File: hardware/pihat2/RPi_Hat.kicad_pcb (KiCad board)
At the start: 2 copper layers, 65 x 56.5 mm, 48 parts, among them J2 RPi_GPIO, P1 USB_OTG, P2 BATT, P3 THERM, U1 MCP73833, U2 SMA_Edge_Mount, U3 SMA_Edge_Mount, U4 TPS61027, U5 MCP3021, U6 Si4464, X1 30MHz

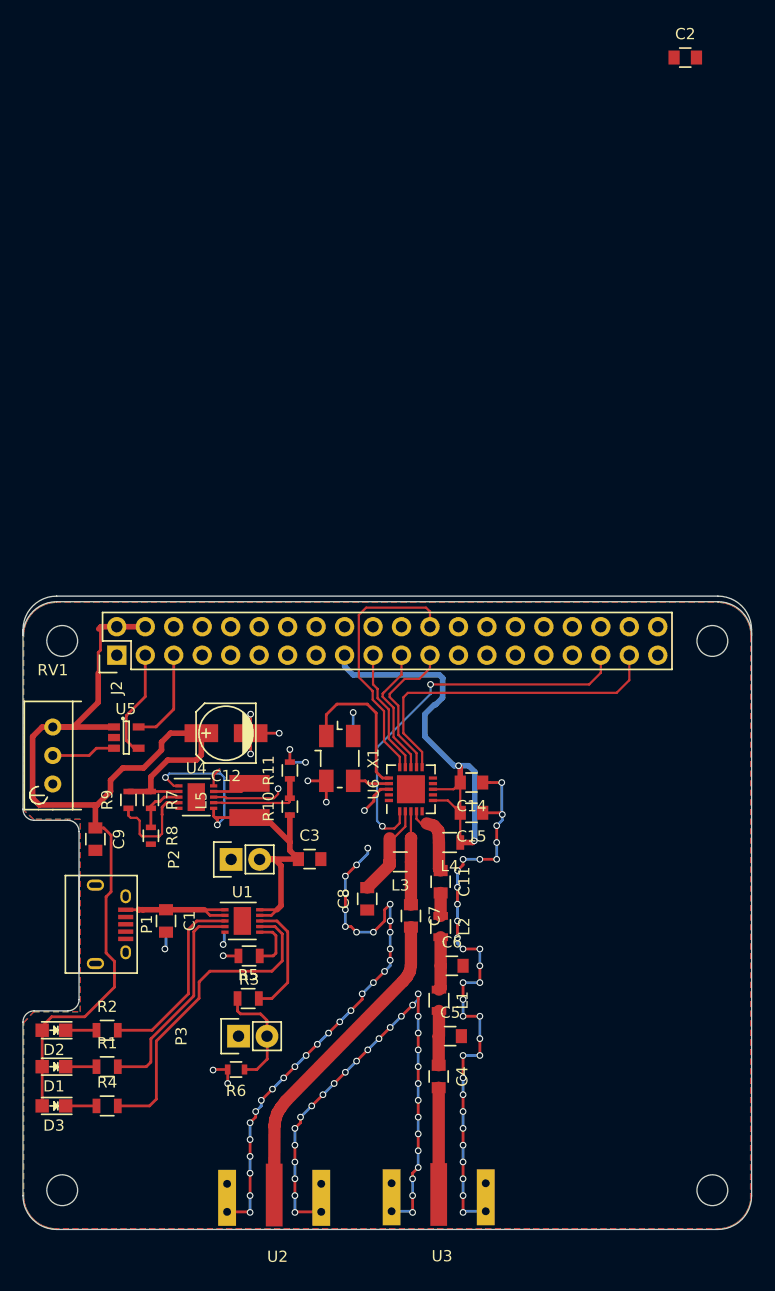
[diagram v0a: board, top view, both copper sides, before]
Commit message: Added some Silkscreen.
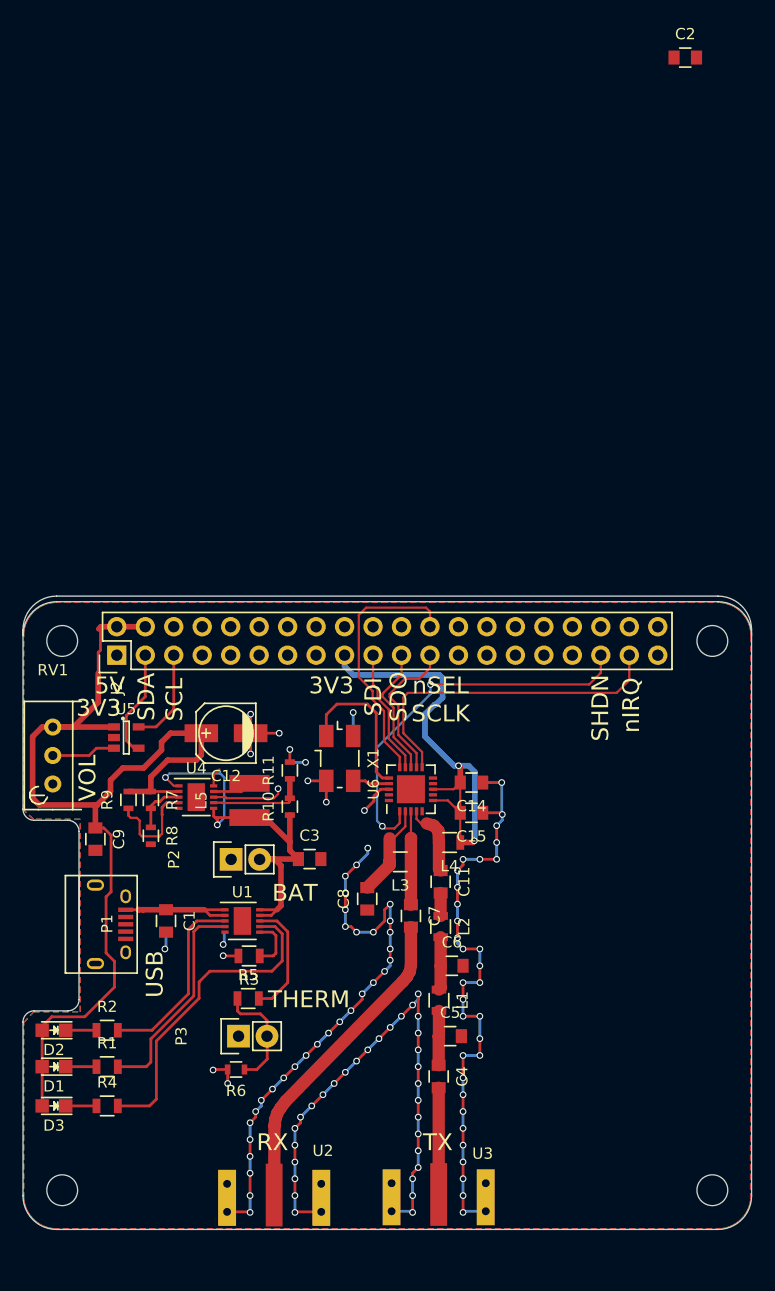
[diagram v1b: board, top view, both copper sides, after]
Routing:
- net (no net): track 0.00 -> 6.13 mm, vias 0 -> 4
- net GND: track 182.2 -> 176.1 mm, vias 110 -> 106
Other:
- board text added: "3V3"
- board text added: "5V"
- board text added: "BAT"
- board text added: "RX"
- board text added: "SCL"
- board text added: "SCLK"
- board text added: "SDA"
- board text added: "SDI"
- board text added: "SDO"
- board text added: "SHDN"
- board text added: "THERM"
- board text added: "TX"
- board text added: "USB"
- board text added: "VOL"
- board text added: "nIRQ"
- board text added: "nSEL"

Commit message: Finished Silkscreen Work.
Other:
- board text added: "+"
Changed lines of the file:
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@@
     (links 114)
     (no_connects 9)
-    (area 74.584999 41.9 139.790001 153.025)
+    (area 74.584999 41.9 139.790001 151.325)
     (thickness 1.6)
-    (drawings 36)
+    (drawings 38)
     (tracks 568)
     (zones 0)
@@
     (tags "capacitor 0805")
     (attr smd)
-    (fp_text reference C3 (at 0 -2.1) (layer F.SilkS)
+    (fp_text reference C3 (at 2.79 -1.58) (layer F.SilkS)
       (effects (font (size 1 1) (thickness 0.15)))
     )
@@
     (tags "capacitor 0805")
     (attr smd)
-    (fp_text reference C5 (at 0 -2.1) (layer F.SilkS)
+    (fp_text reference C5 (at 4.65 -0.075) (layer F.SilkS)
       (effects (font (size 1 1) (thickness 0.15)))
     )
@@
     (tags "capacitor 0805")
     (attr smd)
-    (fp_text reference C6 (at 0 -2.1) (layer F.SilkS)
+    (fp_text reference C6 (at 4.2 0) (layer F.SilkS)
       (effects (font (size 1 1) (thickness 0.15)))
     )
@@
     (tags "capacitor 0805")
     (attr smd)
-    (fp_text reference C7 (at 0 -2.1 270) (layer F.SilkS)
+    (fp_text reference C7 (at 3.05 0.15 270) (layer F.SilkS)
       (effects (font (size 1 1) (thickness 0.15)))
     )
@@
     (tags "capacitor 0805")
     (attr smd)
-    (fp_text reference C9 (at 0 -2.1 270) (layer F.SilkS)
+    (fp_text reference C9 (at 0 -2.7 270) (layer F.SilkS)
       (effects (font (size 1 1) (thickness 0.15)))
     )
@@
     (tags "capacitor 0805")
     (attr smd)
-    (fp_text reference C11 (at 0 -2.1 270) (layer F.SilkS)
+    (fp_text reference C11 (at 0.1 -3.4 270) (layer F.SilkS)
       (effects (font (size 1 1) (thickness 0.15)))
     )
@@
     (descr "SMT capacitor, aluminium electrolytic, 5x5.3")
     (attr smd)
-    (fp_text reference C12 (at 0 -3.81 180) (layer F.SilkS)
+    (fp_text reference C12 (at -0.05 2.55 180) (layer F.SilkS)
       (effects (font (size 1 1) (thickness 0.15)))
     )
@@
     (tags "capacitor 0805")
     (attr smd)
-    (fp_text reference C14 (at 0 -2.1 180) (layer F.SilkS)
+    (fp_text reference C14 (at -4.95 0.05 180) (layer F.SilkS)
       (effects (font (size 1 1) (thickness 0.15)))
     )
@@
     (tags "capacitor 0805")
     (attr smd)
-    (fp_text reference C15 (at 0 -2.1 180) (layer F.SilkS)
+    (fp_text reference C15 (at -4.65 0.05 180) (layer F.SilkS)
       (effects (font (size 1 1) (thickness 0.15)))
     )
@@
     (tags "LED 0805 SMD")
     (attr smd)
-    (fp_text reference D2 (at 0 -1.75 180) (layer F.SilkS)
+    (fp_text reference D2 (at 0 -1.55 180) (layer F.SilkS)
       (effects (font (size 1 1) (thickness 0.15)))
     )
@@
     (tags "resistor 0805")
     (attr smd)
-    (fp_text reference L4 (at 0 -2.1 180) (layer F.SilkS)
+    (fp_text reference L4 (at -3.2 0 180) (layer F.SilkS)
       (effects (font (size 1 1) (thickness 0.15)))
     )
@@
   (module inductor:BOURNES_SRN4018 (layer F.Cu)
     (at 94.95 111.25 270)
-    (fp_text reference L5 (at 0 4.3 270) (layer F.SilkS)
+    (fp_text reference L5 (at 0.05 -0.15 360) (layer F.SilkS)
       (effects (font (size 1 1) (thickness 0.15)))
     )
@@
     (descr "Through hole pin header")
     (tags "pin header")
-    (fp_text reference P2 (at 0 -5.1 90) (layer F.SilkS)
+    (fp_text reference P2 (at 0.01 -2.81 90) (layer F.SilkS)
       (effects (font (size 1 1) (thickness 0.15)))
     )
@@
     (tags "resistor 0805")
     (attr smd)
-    (fp_text reference R1 (at 0 -2.1) (layer F.SilkS)
+    (fp_text reference R1 (at 0.05 1.7) (layer F.SilkS)
       (effects (font (size 1 1) (thickness 0.15)))
     )
@@
     (tags "resistor 0805")
     (attr smd)
-    (fp_text reference R2 (at 0 -2.1) (layer F.SilkS)
+    (fp_text reference R2 (at -0.05 1.65) (layer F.SilkS)
       (effects (font (size 1 1) (thickness 0.15)))
     )
@@
     (tags "resistor 0805")
     (attr smd)
-    (fp_text reference R4 (at 0 -2.1) (layer F.SilkS)
+    (fp_text reference R4 (at 0.05 2) (layer F.SilkS)
       (effects (font (size 1 1) (thickness 0.15)))
     )
@@
     (tags "resistor 0603")
     (attr smd)
-    (fp_text reference R7 (at 0 -1.9 270) (layer F.SilkS)
+    (fp_text reference R7 (at -2.5 -0.05 270) (layer F.SilkS)
       (effects (font (size 1 1) (thickness 0.15)))
     )
@@
     (tags "QFN 0.5")
     (attr smd)
-    (fp_text reference U6 (at 0 -3.33 90) (layer F.SilkS)
+    (fp_text reference U6 (at 3.55 0.15 90) (layer F.SilkS)
       (effects (font (size 1 1) (thickness 0.15)))
     )
@@
     (tags "crystal oscillator quartz SMD SMT 5032")
     (attr smd)
-    (fp_text reference X1 (at 0 -3 270) (layer F.SilkS)
+    (fp_text reference X1 (at 4.7 0 270) (layer F.SilkS)
       (effects (font (size 1 1) (thickness 0.15)))
     )
@@
     (tags SOT-23-5)
     (attr smd)
-    (fp_text reference U5 (at -0.05 -2.55) (layer F.SilkS)
+    (fp_text reference U5 (at 2.74 -0.04) (layer F.SilkS)
       (effects (font (size 1 1) (thickness 0.15)))
     )
@@
     )
   )
+  (gr_text + (at 98.1 114.2) (layer F.SilkS)
+    (effects (font (size 1.5 1.5) (thickness 0.3)))
+  )
+  (gr_text + (at 99.1 132.2) (layer F.SilkS)
+    (effects (font (size 1.5 1.5) (thickness 0.3)))
+  )
   (gr_text 3V3 (at 81.5 103) (layer F.SilkS)

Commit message: Worked on RF Layout.
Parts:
- removed C2: 10uF, Capacitors_SMD:C_0805
- removed X1: 30MHz, Crystals:Crystal_SMD_5032_4Pads
- added C10: C, Capacitors_SMD:C_0805, B.Cu at (98.5, 103.4)
- added C13: C, Capacitors_SMD:C_0805, B.Cu at (98.6, 113.7)
- added Y1: Crystal, Crystals:Crystal_HC49-SD_SMD, B.Cu at (102.5, 108.6)
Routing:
- net +3V3: track 41.9 -> 64.2 mm
- net Net-(C10-Pad2): track 3.29 -> 14.3 mm, vias 0 -> 1
- net GND: track 176.1 -> 172.5 mm, vias 106 -> 103
- net (no net): track 6.13 -> 2.68 mm, vias 4 -> 2
- net Net-(C13-Pad2): track 13.7 -> 10.4 mm, vias 0 -> 1
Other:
- board size 65 x 56.5 mm -> 65 x 56 mm

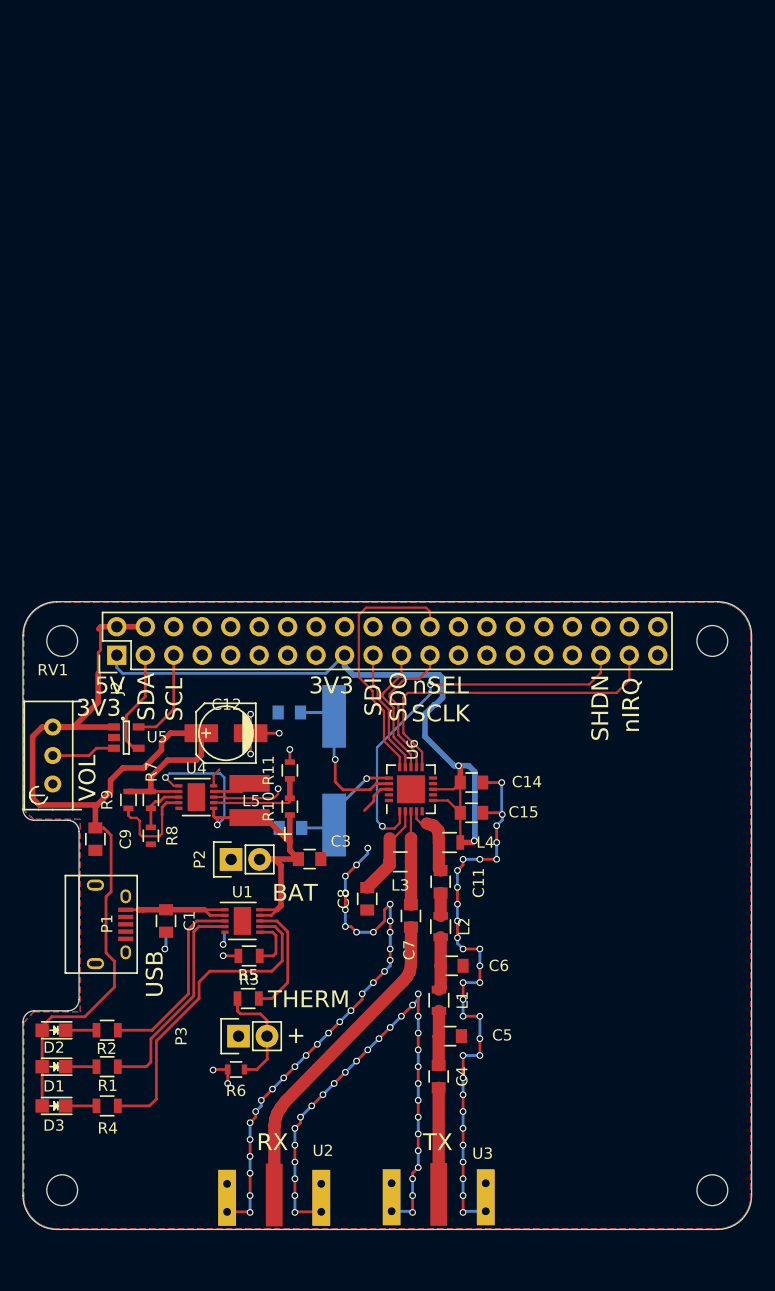
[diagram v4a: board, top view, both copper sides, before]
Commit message: Minor changes to pihat 2 in prep for boardhouse #2.
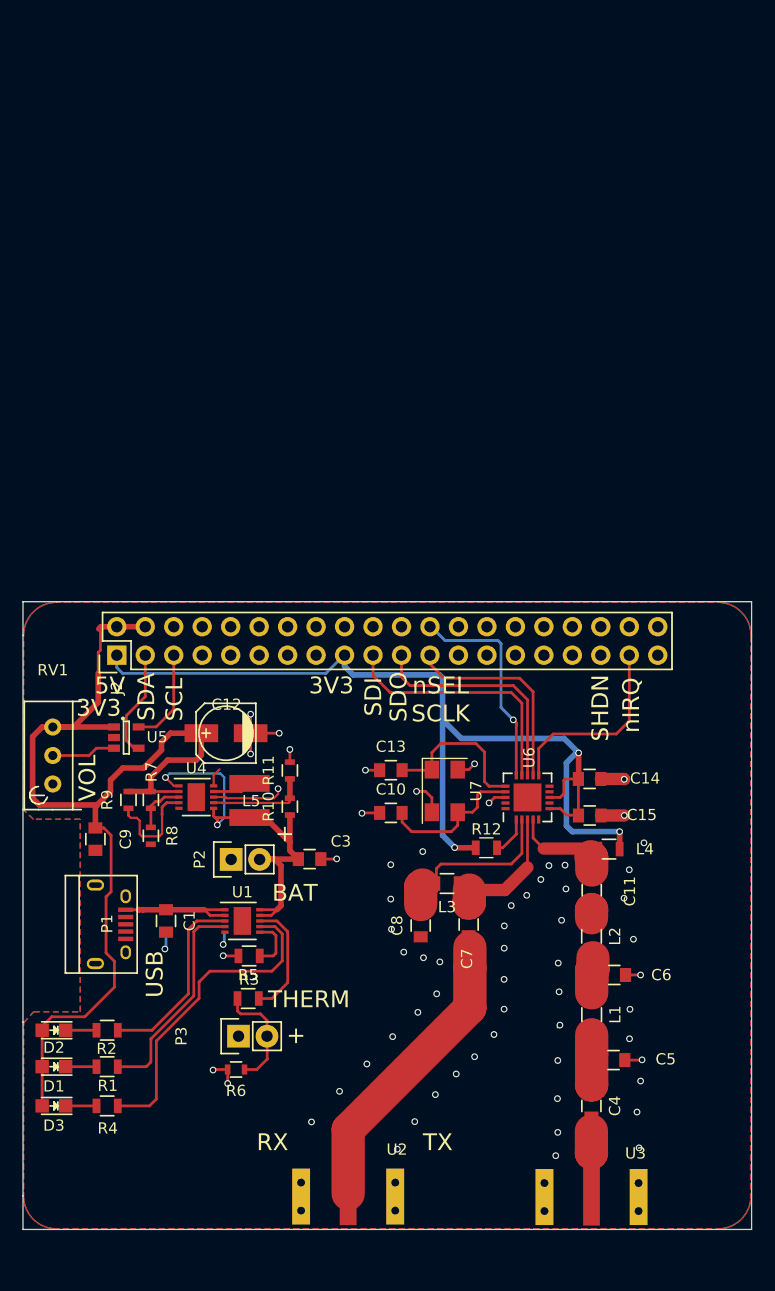
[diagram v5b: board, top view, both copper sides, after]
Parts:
- removed ? (x4): , RPi_Hat:RPi_Hat_Mounting_Hole
- removed Y1: Crystal, Crystals:Crystal_HC49-SD_SMD
- added R12: 1K, Resistors_SMD:R_0805, F.Cu at (116.1, 115.5)
- added U7: 30MHz, Crystals:Crystal_SMD_Abracon_ABM3C-4pin_5.0x3.2mm, F.Cu at (112.4, 110.4)
- C10, C13: value C -> 12pF; moved to F.Cu
- moved C5 14.7 mm to (127.4, 134.4)
- moved C6 14.5 mm to (127.5, 126.8)
- moved L4 14.2 mm to (127.0, 115.6)
- moved C4 13.9 mm to (125.5, 138.5)
- moved L1 13.7 mm to (125.5, 130.3)
- moved U3 13.6 mm to (125.5, 146.4)
- moved C11 13.5 mm to (125.5, 119.2)
- moved L2 13.5 mm to (125.5, 123.4)
- moved C10 12.7 mm to (107.6, 112.4)
- moved C15 10.6 mm to (125.3, 112.6)
- moved C14 10.5 mm to (125.3, 109.3)
- moved U6 10.4 mm to (119.8, 111.0)
- moved C13 10.3 mm to (107.6, 108.5)
- moved U2 6.60 mm to (103.8, 146.3)
- moved C8 5.33 mm to (110.2, 122.4)
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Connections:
- J2 pad 35: SHDN -> (no net)
- U6 pad 1: SHDN -> Net-(R12-Pad2)
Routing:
- net GND: track 172.5 -> 36.9 mm, vias 103 -> 18
- net SHDN: track 34.9 -> 0.00 mm, vias 2 -> 0
- net +3V3: track 64.2 -> 89.1 mm, vias 2 -> 3
- net nIRQ: track 29.9 -> 17.4 mm
- net SDI: track 12.5 -> 23.9 mm
- net SDO: track 11.7 -> 20.8 mm
- net Net-(C8-Pad2): track 8.49 -> 16.7 mm
- net Net-(C7-Pad1): track 8.37 -> 13.7 mm
- net SCLK: track 13.2 -> 18.5 mm
- net Net-(C11-Pad1): track 6.65 -> 10.9 mm
- net nSEL: track 23.2 -> 19.3 mm, vias 0 -> 1
- net Net-(C13-Pad2): track 10.4 -> 14.2 mm, vias 1 -> 0
- net Net-(R12-Pad2): track 0.00 -> 3.54 mm
- net Net-(C4-Pad1): track 4.86 -> 7.75 mm
- net TXO: track 9.53 -> 6.90 mm
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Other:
- outline, holes or cut-outs redrawn

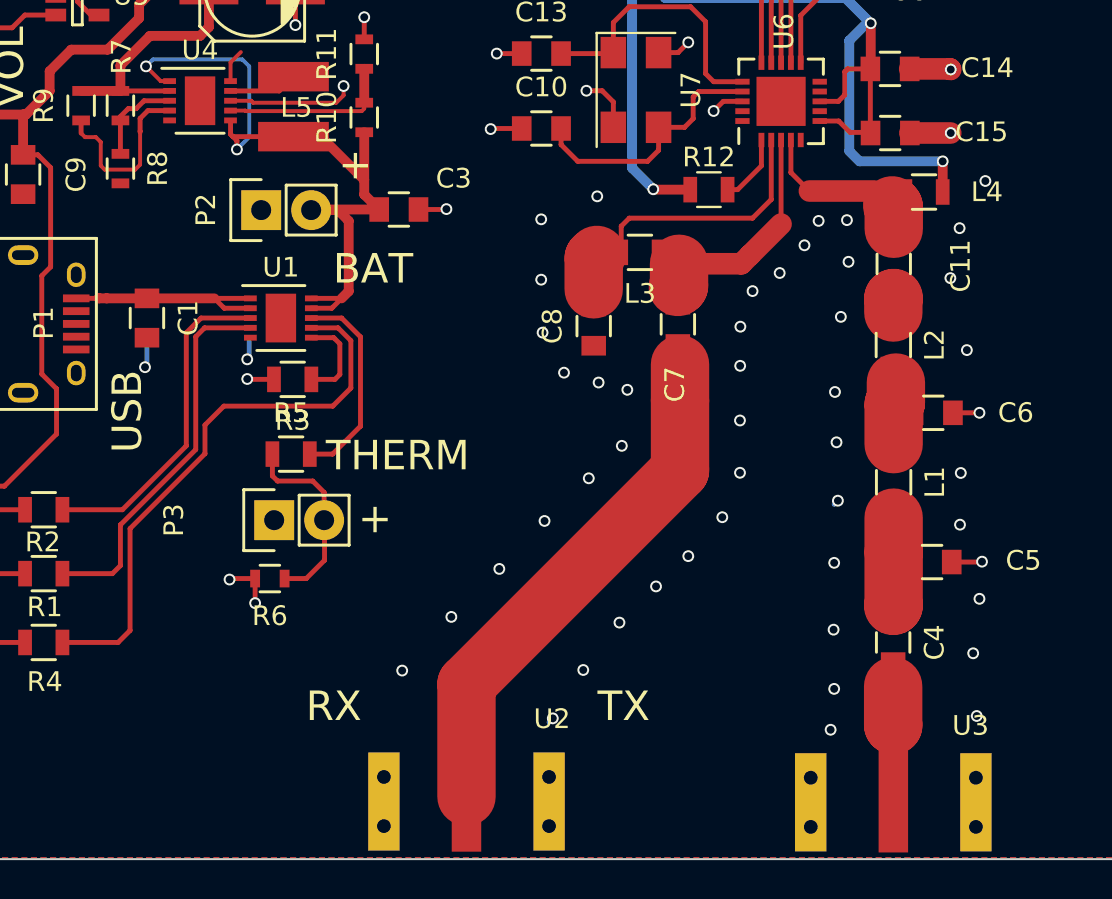
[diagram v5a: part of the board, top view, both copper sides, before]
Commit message: Re-Established Vias.
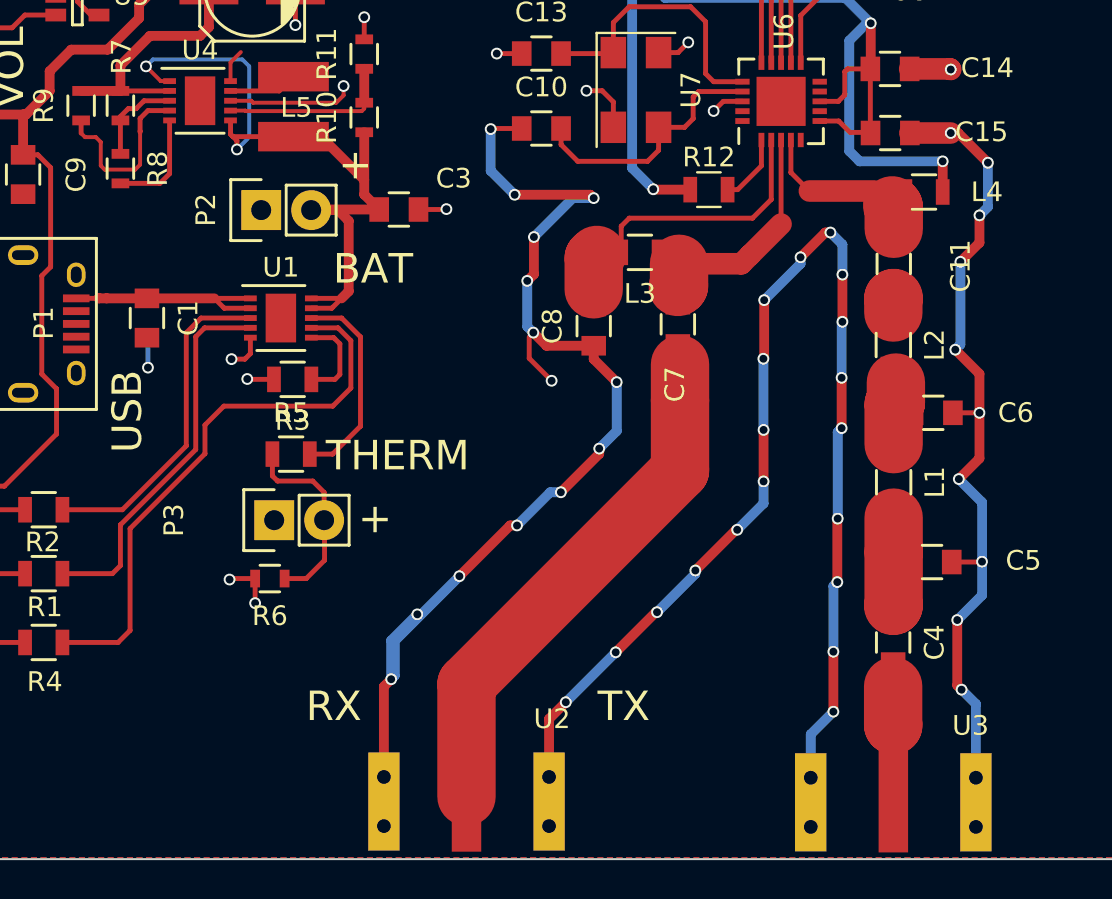
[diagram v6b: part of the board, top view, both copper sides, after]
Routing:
- net GND: track 36.9 -> 199.7 mm, vias 18 -> 59
- net (no net): track 4.45 -> 0.00 mm, vias 48 -> 0
